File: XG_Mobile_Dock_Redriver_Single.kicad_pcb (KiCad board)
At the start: 6 copper layers, 220.1 x 93 mm, 156 parts, among them J1 5-1775443-8, J10 SWD, J11 UART, J12 I2C1, J13 39301240, J14 I2C1, J2 20455-040E-76, J3 20455-040E-76, J4 469911008, J7 10147430-113T0LF, Q16 AO3401A, Q17 2N7002W, SW1 SW_Push, U1 DS320PR810NJXR, U12 STM32F030C8Tx, U7 TPS7A8400ARGRR, U8 TPS7A8400ARGRR

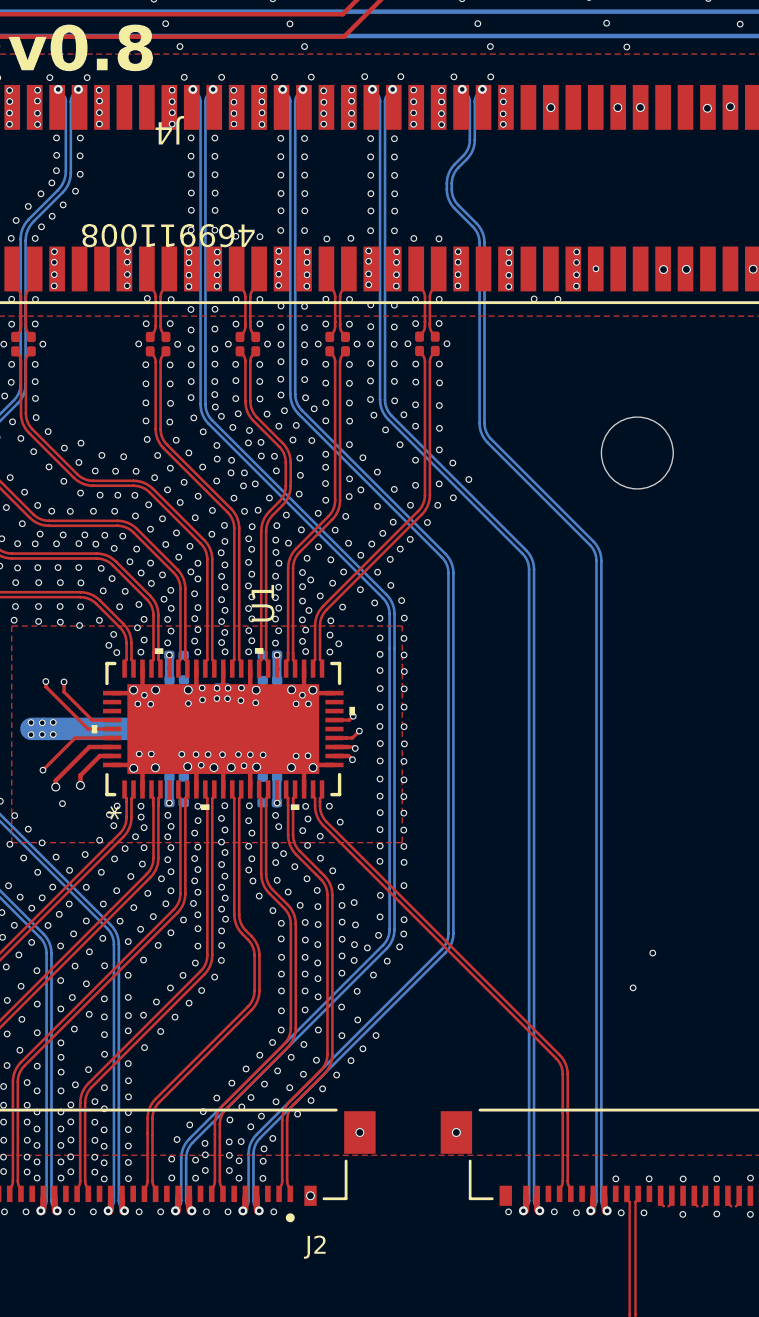
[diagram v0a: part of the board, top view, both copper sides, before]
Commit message: Update XG_Mobile_Dock_Redriver_Single.kicad_pcb
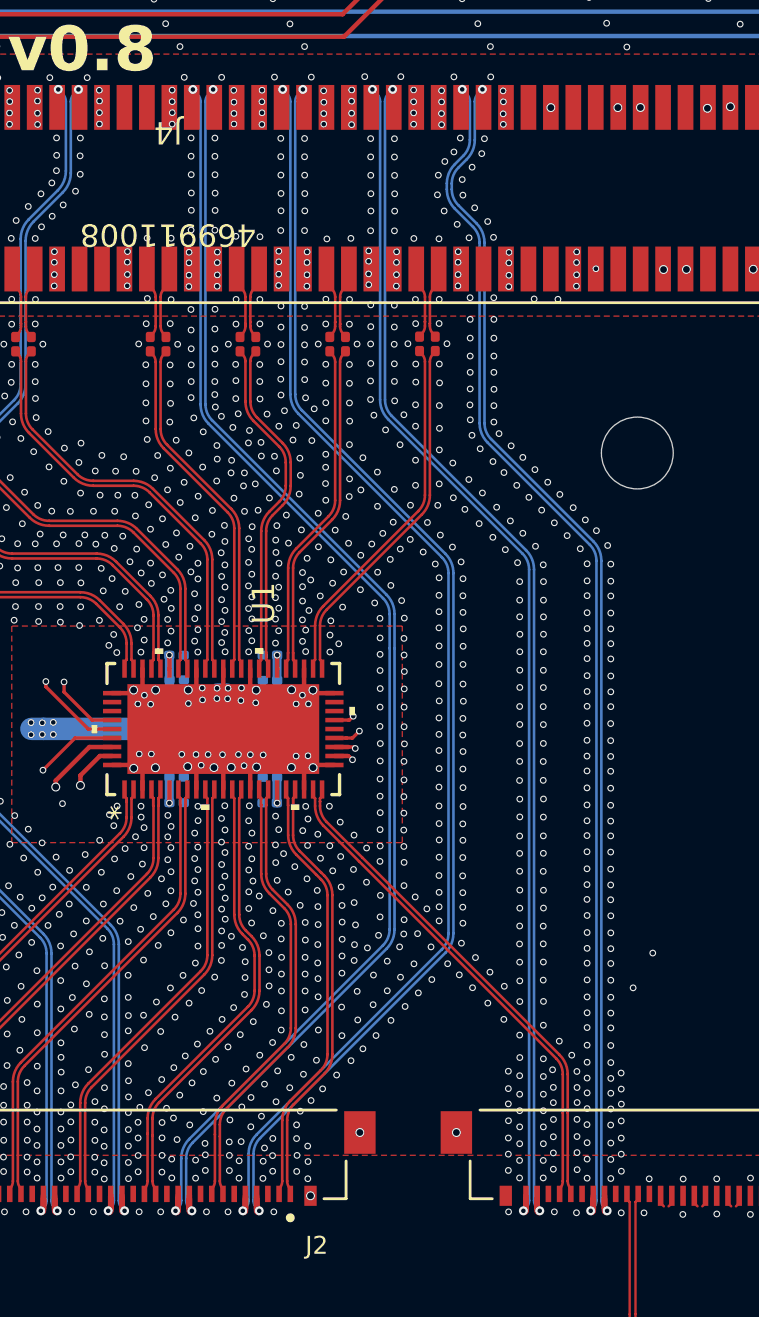
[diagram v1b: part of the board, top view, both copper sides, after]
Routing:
- net GND: vias 2197 -> 2557
